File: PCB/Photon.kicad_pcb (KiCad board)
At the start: 2 copper layers, 21.2 x 74.4 mm, 45 parts, among them J1 USB_C_Receptacle_USB2.0_6P, J2 Conn_01x05_Socket, Q1 IRLML6402, Q2 IRLML6402, SW1 TS-1088-AR02016, U1 STM32G030F6P6TR, U2 TP4056, U3 RT8059GJ5, U4 DW01A, U5 FS8205A, U6 BCR421UW6-7, U7 BCR421UW6-7

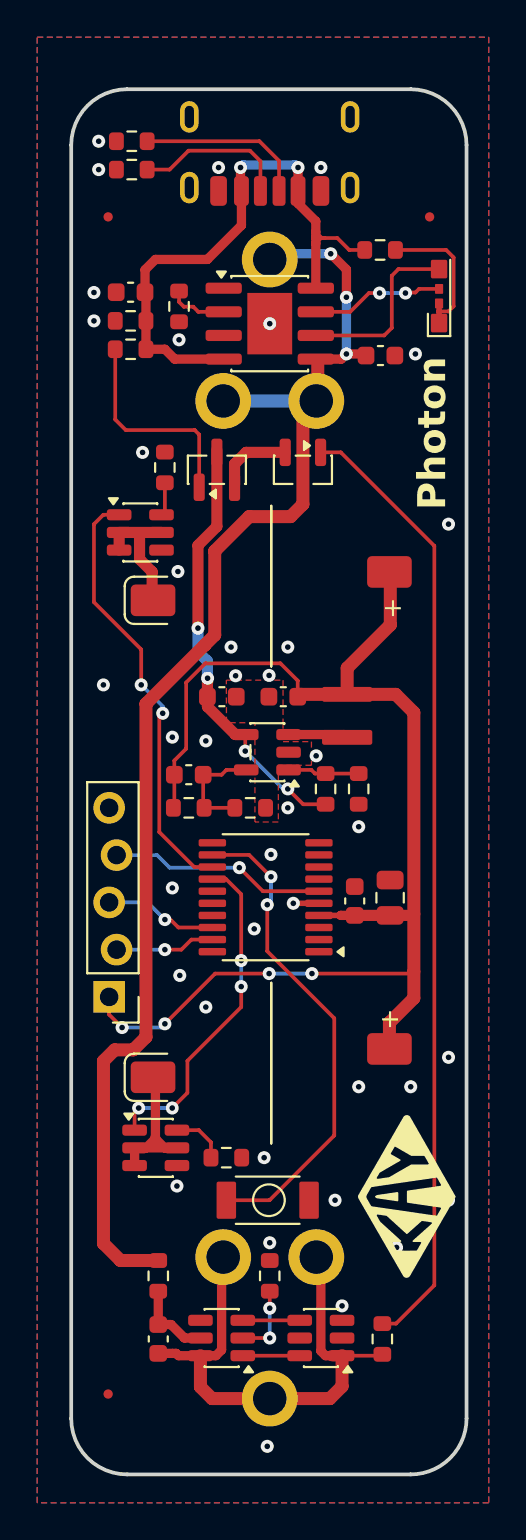
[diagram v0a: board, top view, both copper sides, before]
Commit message: Schematic, Board and Firmware changes
Moved pins for LEDs onto timer channel capable pins to allow for future implementation if desired

Added 100nF cap to NRST pin

Changed programming footprint to use soic8 programmers found on Github

Changed buck to diodes fixed version (AP63203WU) for fewer components

Created Gerbers

Updated .ioc for pinout using timer channels and naming pins to match

Added footprint for debugger
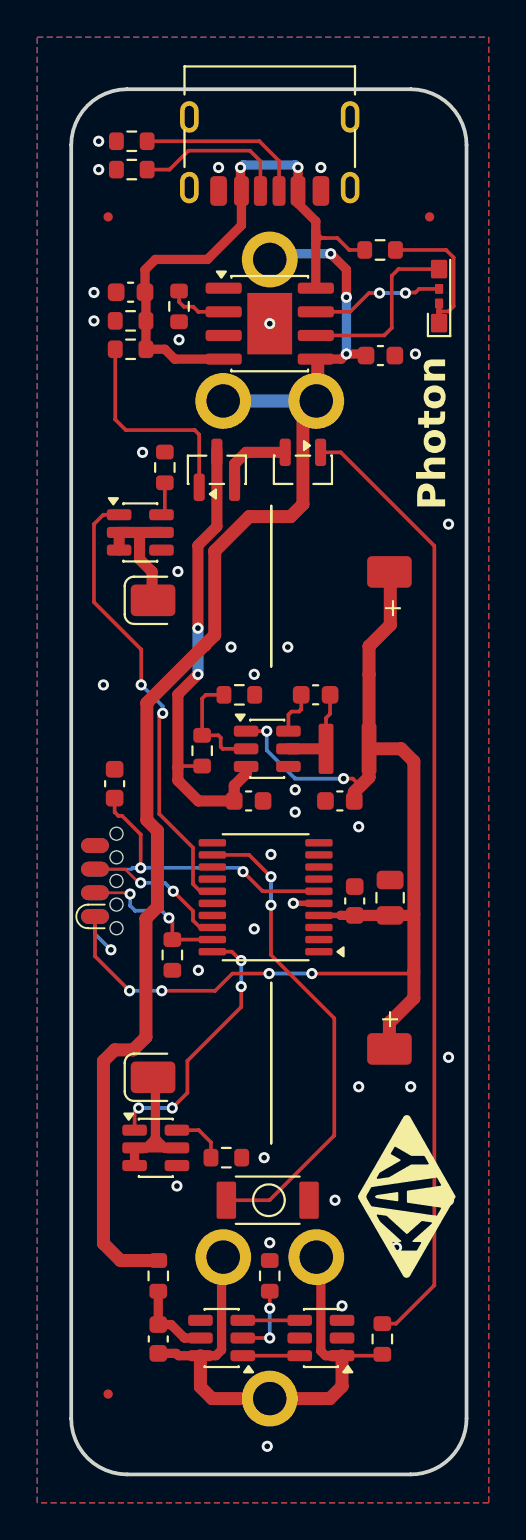
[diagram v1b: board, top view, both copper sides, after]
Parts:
- removed C7: 10uF, Capacitor_SMD:C_0603_1608Metric
- removed R10: 62K, Resistor_SMD:R_0603_1608Metric
- added C10: 100nF, Capacitor_SMD:C_0603_1608Metric, F.Cu at (41.1, 60.9)
- added C9: 22uF, Capacitor_SMD:C_0603_1608Metric, F.Cu at (53.2, 61.8)
- C6: value 10pF -> 100nF
- J2: value Conn_01x05_Socket -> SOIC 8 Debug Clip; footprint Connector_PinHeader_2.54mm:PinHeader_1x05_P2.54mm_Vertical -> SOIC Debug 8 ConN:SOIC_clipProgSmall
- L1: value 2.2uH -> 4.7uH
- R5: value 12K -> 180K
- R6: value 10K -> 100K
- R9: value 280K -> 10K
- U3: value RT8059GJ5 -> AP63203WU; footprint Package_TO_SOT_SMD:SOT-23-5 -> Package_TO_SOT_SMD:TSOT-23-6
- moved R6 8.17 mm to (47.8, 56.1), turned to 0 degrees
- moved C6 8.06 mm to (51.9, 56.1)
- moved R9 7.95 mm to (44.2, 70.1), turned to -90 degrees
- moved R5 6.95 mm to (45.8, 59.1)
- moved J2 6.46 mm to (39.3, 66.1), turned to -90 degrees
- moved C4 5.78 mm to (48.3, 61.8)
- moved L1 1.66 mm to (53.6, 58.9), turned to 0 degrees
- moved U3 0.18 mm to (49.3, 59.0), turned to 0 degrees
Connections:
- C6 pad 1: /FB -> /SW
- C6 pad 2: +3V3 -> /BST
- J2 pad 4: NRST -> unconnected-(J2-Pin_4-Pad4)
- J2 pad 5: GND -> unconnected-(J2-Pin_5-Pad5)
- L1 pad 1: /LX -> /SW
- R9 pad 1: +3V3 -> SWCLK
- R9 pad 2: /FB -> GND
- U1 pad 13: LED1_EN -> unconnected-(U1-PA6-Pad13)
- U1 pad 14: LED2_EN -> unconnected-(U1-PA7-Pad14)
- U1 pad 15: unconnected-(U1-PA8/PB0/PB1/PB2-Pad15) -> LED1_EN
- U1 pad 20: unconnected-(U1-PB3/PB4/PB5/PB6-Pad20) -> LED2_EN
- U3 pad 1: /UVLO -> +3V3
- U3 pad 2: GND -> /UVLO
- U3 pad 3: /LX -> /VBAT_SYS
- U3 pad 4: /VBAT_SYS -> GND
- U3 pad 5: /FB -> /SW
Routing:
- net /FB: track 5.66 -> 0.00 mm
- net +3V3: track 70.9 -> 65.3 mm, vias 4 -> 6
- net NRST: track 11.7 -> 17.0 mm, vias 1 -> 2
- net /SW: track 0.00 -> 5.01 mm
- net LED2_EN: track 18.1 -> 14.4 mm
- net /LX: track 3.29 -> 0.00 mm
- net SWCLK: track 5.37 -> 8.29 mm, vias 1 -> 2
- net /BST: track 0.00 -> 2.47 mm
- net /UVLO: track 3.86 -> 6.19 mm
- net GND: track 1.38 -> 3.53 mm, vias 39 -> 35
- net /VBAT_SYS: track 23.5 -> 25.5 mm, vias 4 -> 2
- net SWDIO: track 5.90 -> 7.90 mm, vias 1 -> 2
- net LED1_EN: track 23.3 -> 24.5 mm

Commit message: updated silkscreen to match gerbers
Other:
- board text added: "V7 04-07-2026"
- board text removed: "V6 02-15-2026"
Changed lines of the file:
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@@
 		)
 	)
-	(gr_text "V6 02-15-2026\n\n"
+	(gr_text "V7 04-07-2026\n\n"
 		(at 46.9 77.175 90)
 		(layer "B.SilkS")

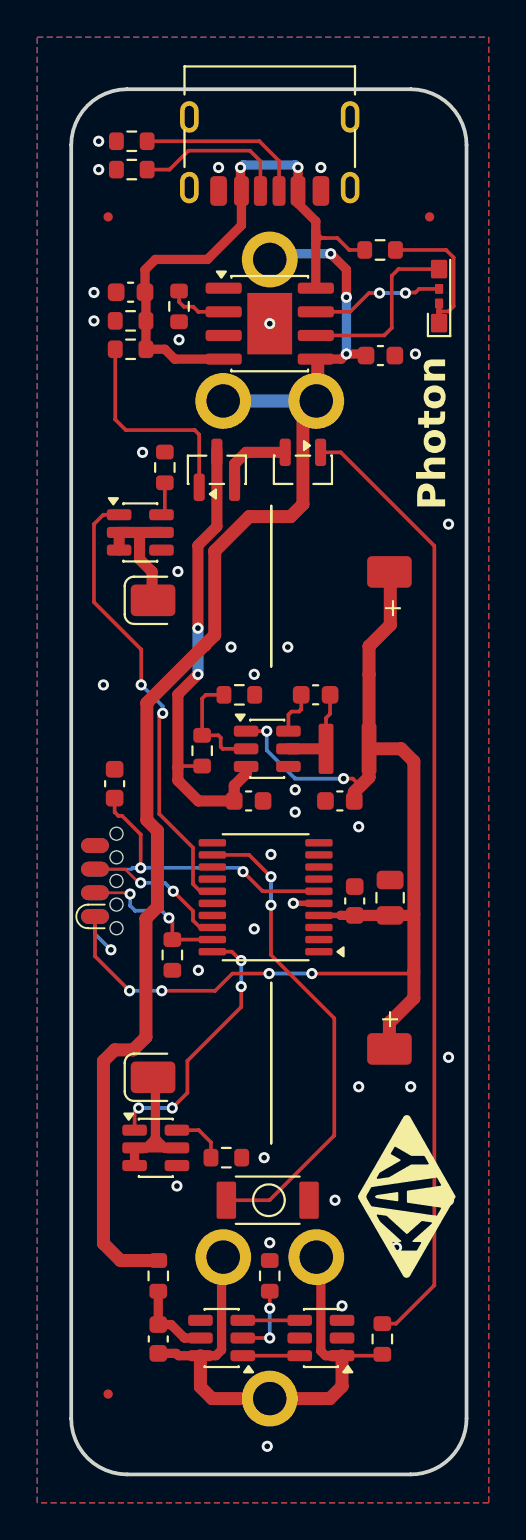
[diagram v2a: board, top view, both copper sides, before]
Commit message: Component changes for better button and LED
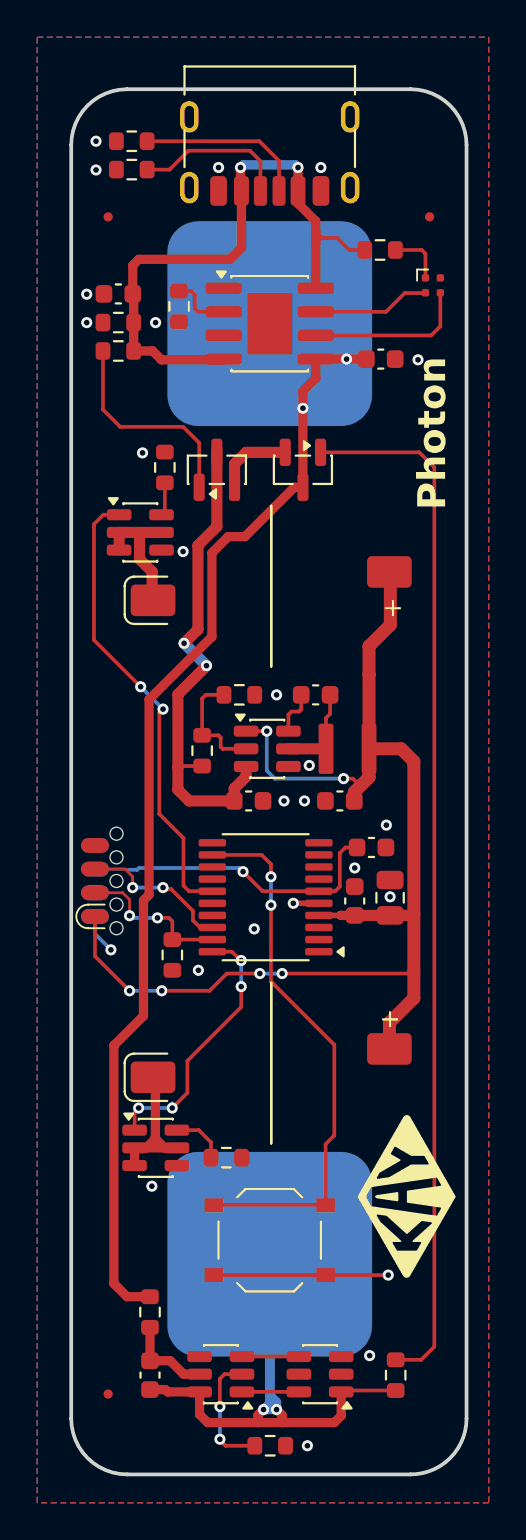
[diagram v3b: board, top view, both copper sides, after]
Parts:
- BT1: footprint Photon:Spring Battery TH -> Photon:18650 Tin Strips
- D1: value LED_Dual_AKAK -> XL-1010RGB-YG; footprint Photon:3.9mm Bi directional side mount LED -> LED_SMD:LED_Wurth_150044M155260
- SW1: footprint Photon:5mm Push Button -> Button_Switch_SMD:SW_Push_1P1T_XKB_TS-1187A
- moved C10 14.2 mm to (54.9, 64.3), turned to 180 degrees
- moved R13 9.13 mm to (49.5, 96.4), turned to 180 degrees
- moved BT1 6.15 mm to (50.0, 36.2)
- moved SW1 2.15 mm to (49.4, 85.4)
- moved R14 2.07 mm to (56.2, 92.7)
- moved C8 1.99 mm to (43.0, 92.7)
- moved R11 1.99 mm to (43.0, 89.3)
- moved U4 1.94 mm to (46.8, 92.6)
- moved U5 1.94 mm to (52.1, 92.6)
- moved D1 0.94 mm to (58.2, 34.1), turned to 0 degrees
- moved R7 0.66 mm to (41.3, 37.6)
- moved C3 0.66 mm to (41.3, 34.6)
- moved R8 0.66 mm to (41.3, 36.1)
- moved C5 0.19 mm to (55.4, 38.1)
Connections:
- D1 pad 2: /CHRG -> unconnected-(D1-BK-Pad2)
- D1 pad 3: /LED_PWR -> /CHRG
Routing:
- net +BATT: track 76.1 -> 66.1 mm, vias 3 -> 2
- net GND: track 3.53 -> 12.9 mm, vias 35 -> 25
- net /Bat-: track 27.1 -> 35.4 mm, vias 0 -> 2
- net /LED_PWR: track 8.23 -> 3.00 mm
- net /BAT_DSBL: track 51.6 -> 56.1 mm
- net /BUTN: track 26.2 -> 29.3 mm
- net /VM: track 3.75 -> 6.58 mm
- net 5V: track 32.2 -> 34.5 mm
- net /VBAT_SYS: track 25.5 -> 26.8 mm
- net /STDBY: track 9.74 -> 8.69 mm
- net /CHRG: track 7.13 -> 6.31 mm, vias 2 -> 0
- net +3V3: track 65.3 -> 65.9 mm
- net NRST: track 17.0 -> 16.7 mm, vias 2 -> 1
